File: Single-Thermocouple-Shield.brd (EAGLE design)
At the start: 53.3 x 68.6 mm, 20 parts, among them U1 TXB0104

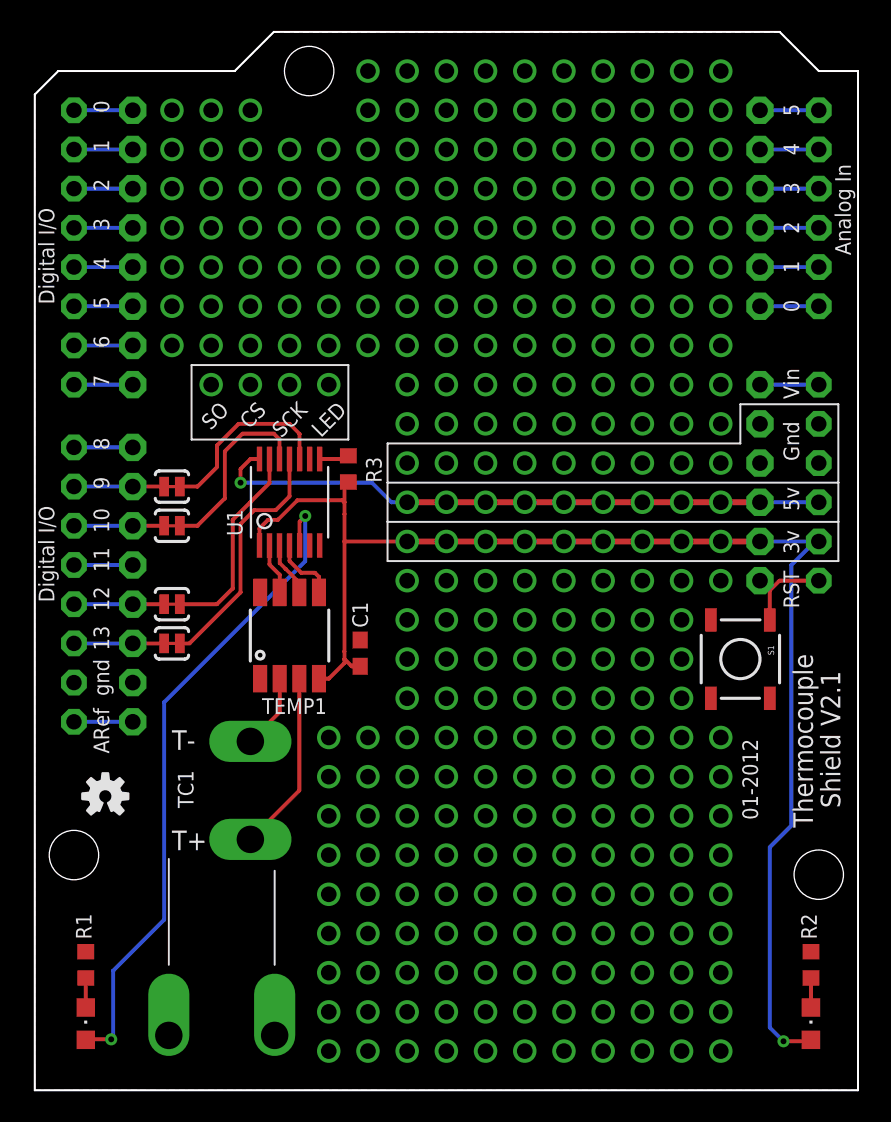
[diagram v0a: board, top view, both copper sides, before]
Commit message: Removed routing of LED through level shifter
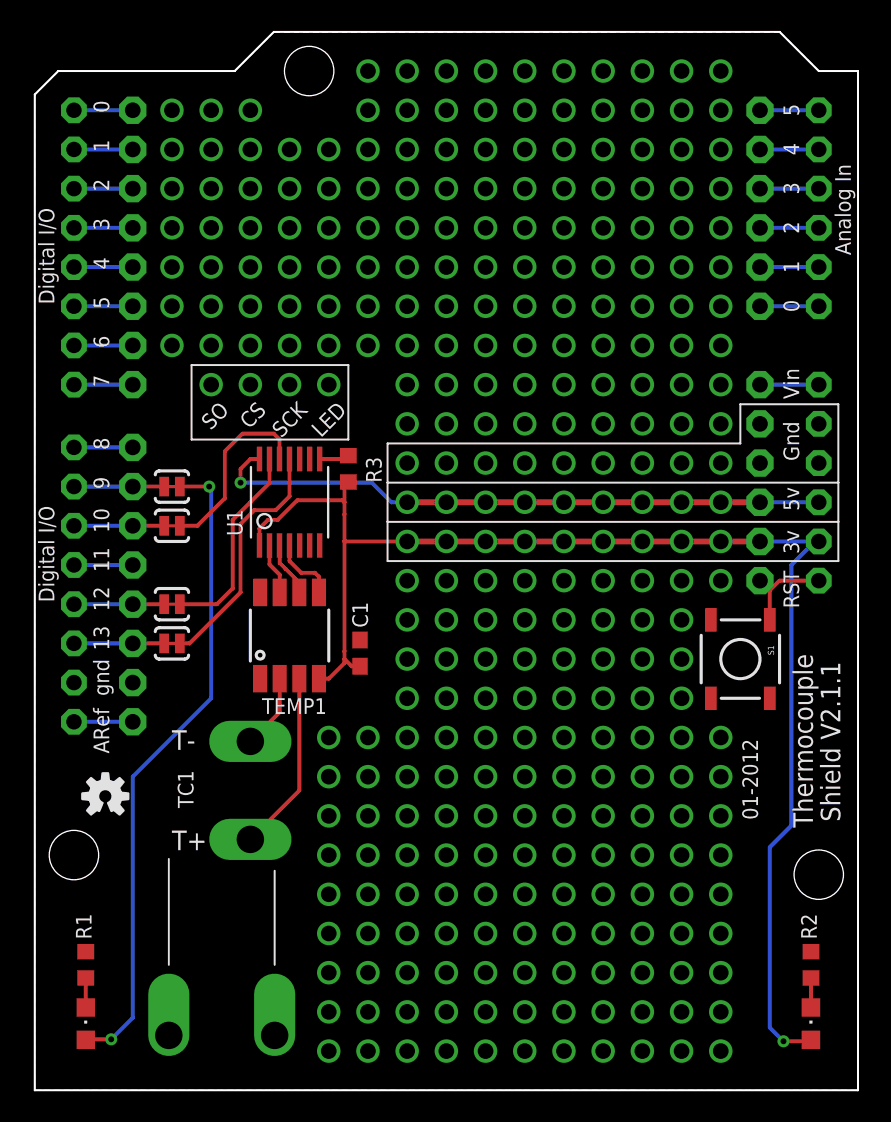
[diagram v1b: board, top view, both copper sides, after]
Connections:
- removed net STATUS: D1.A, U1.5
- net _STATUS: now also D1.A; no longer U1.10
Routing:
- net STATUS: track 42.8 -> 0.00 mm, vias 2 -> 0
- net _STATUS: track 12.2 -> 42.1 mm, vias 0 -> 2
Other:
- board text added: "Shield V2.1.1"
- board text removed: "Shield V2.1"
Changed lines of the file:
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@@
 <text x="17.018" y="44.704" size="1.016" layer="25" font="vector" rot="R225">SCK</text>
 <text x="19.558" y="44.704" size="1.016" layer="25" font="vector" rot="R225">LED</text>
-<text x="52.197" y="18.288" size="1.27" layer="21" rot="SR90">Shield V2.1</text>
+<text x="52.197" y="17.399" size="1.27" layer="21" rot="SR90">Shield V2.1.1</text>
 <rectangle x1="0" y1="22.86" x2="0.635" y2="64.77" layer="41"/>
 <rectangle x1="52.705" y1="31.75" x2="53.34" y2="66.04" layer="41"/>
@@
 <wire x1="47.625" y1="32.385" x2="48.26" y2="33.02" width="0.254" layer="1"/>
 </signal>
-<signal name="STATUS">
-<contactref element="U1" pad="5"/>
+<signal name="_STATUS">
+<contactref element="SJ4" pad="1"/>
 <contactref element="D1" pad="A"/>
-<wire x1="17.16" y1="36.845" x2="17.16" y2="35.3" width="0.254" layer="1"/>
-<wire x1="17.526" y1="37.211" x2="17.16" y2="36.845" width="0.254" layer="1"/>
-<wire x1="17.526" y1="34.29" x2="17.526" y2="37.211" width="0.254" layer="16"/>
-<wire x1="8.382" y1="25.146" x2="17.526" y2="34.29" width="0.254" layer="16"/>
-<wire x1="8.382" y1="11.049" x2="8.382" y2="25.146" width="0.254" layer="16"/>
-<wire x1="5.08" y1="7.747" x2="8.382" y2="11.049" width="0.254" layer="16"/>
-<wire x1="5.08" y1="3.429" x2="5.08" y2="7.747" width="0.254" layer="16"/>
-<wire x1="4.953" y1="3.302" x2="5.08" y2="3.429" width="0.254" layer="16"/>
 <wire x1="3.336" y1="3.302" x2="4.953" y2="3.302" width="0.254" layer="1"/>
 <wire x1="3.302" y1="3.268" x2="3.336" y2="3.302" width="0.254" layer="1"/>
-<via x="17.526" y="37.211" extent="1-16" drill="0.381" diameter="0.7874"/>
 <via x="4.953" y="3.302" extent="1-16" drill="0.381" diameter="0.7874"/>
-</signal>
-<signal name="_STATUS">
-<contactref element="U1" pad="10"/>
-<contactref element="SJ4" pad="1"/>
-<wire x1="17.16" y1="42.53" x2="17.16" y2="40.9" width="0.254" layer="1"/>
-<wire x1="16.51" y1="43.18" x2="17.16" y2="42.53" width="0.254" layer="1"/>
-<wire x1="13.208" y1="43.18" x2="16.51" y2="43.18" width="0.254" layer="1"/>
-<wire x1="11.811" y1="41.783" x2="13.208" y2="43.18" width="0.254" layer="1"/>
-<wire x1="11.811" y1="40.386" x2="11.811" y2="41.783" width="0.254" layer="1"/>
-<wire x1="10.541" y1="39.116" x2="11.811" y2="40.386" width="0.254" layer="1"/>
-<wire x1="9.398" y1="39.116" x2="10.541" y2="39.116" width="0.254" layer="1"/>
+<wire x1="4.953" y1="3.302" x2="6.35" y2="4.699" width="0.254" layer="16"/>
+<wire x1="6.35" y1="4.699" x2="6.35" y2="20.32" width="0.254" layer="16"/>
+<wire x1="6.35" y1="20.32" x2="11.43" y2="25.4" width="0.254" layer="16"/>
+<wire x1="11.43" y1="25.4" x2="11.43" y2="38.989" width="0.254" layer="16"/>
+<wire x1="11.43" y1="38.989" x2="11.303" y2="39.116" width="0.254" layer="16"/>
+<via x="11.303" y="39.116" extent="1-16" drill="0.381"/>
+<wire x1="11.303" y1="39.116" x2="9.398" y2="39.116" width="0.254" layer="1"/>
 </signal>
 <signal name="CS">
